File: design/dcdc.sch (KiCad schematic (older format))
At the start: 23 parts

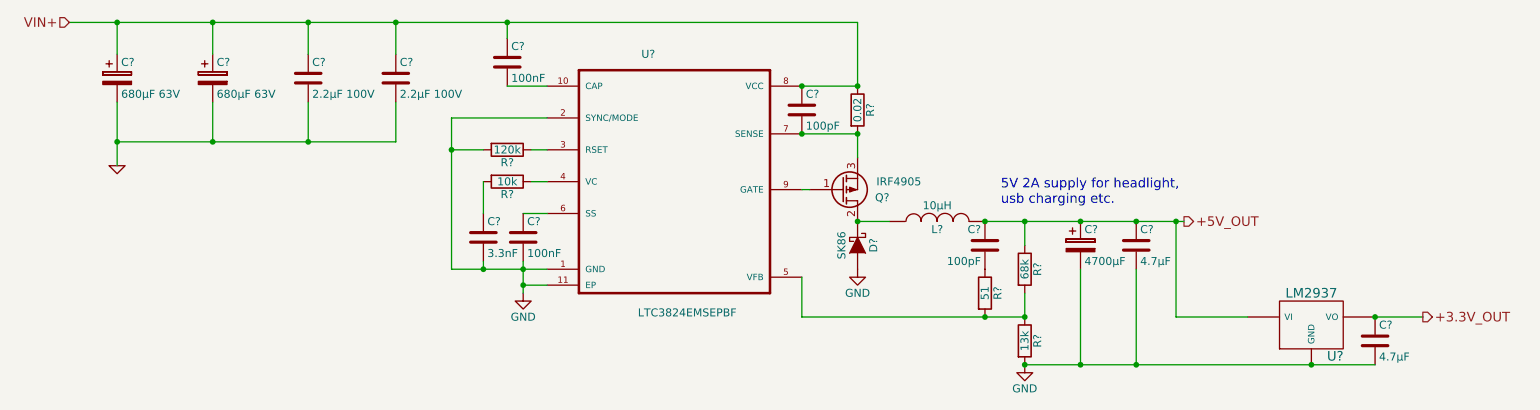
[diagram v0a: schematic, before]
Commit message: schema mods done
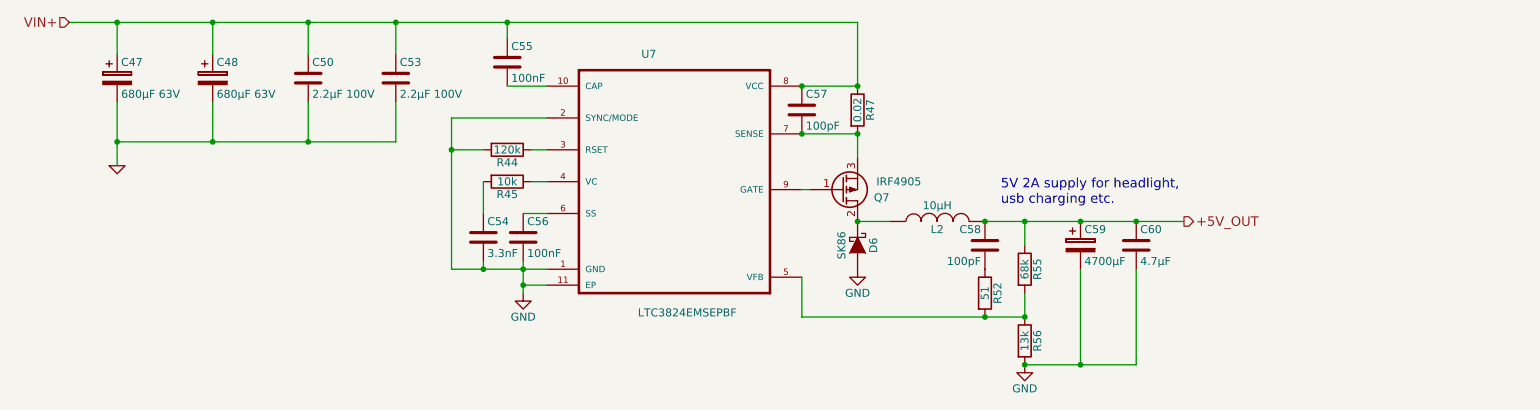
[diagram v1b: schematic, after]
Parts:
- removed C?: 4.7µF, Capacitors_SMD:C_1210, symbol C
- removed U?: LM2937, symbol LM2937
- gave numbers to parts that had none: 21
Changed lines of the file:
@@
 LIBS:LTC3824EMSEPBF
 LIBS:lm2937
+LIBS:bluetooth_spp-ca
+LIBS:microsd
+LIBS:lsm303d
+LIBS:lsm6ds3
 LIBS:BLDC_4-cache
 EELAYER 25 0
@@
 VIN+
 $Comp
-L CP C?
+L CP C47
 U 1 1 562DF65C
 P 1650 2500
-F 0 "C?" H 1675 2600 50  0000 L CNN
+F 0 "C47" H 1675 2600 50  0000 L CNN
 F 1 "680µF 63V" H 1675 2400 50  0000 L CNN
 F 2 "" H 1688 2350 30  0000 C CNN
@@
 $EndComp
 $Comp
-L CP C?
+L CP C48
 U 1 1 562DF6B6
 P 2250 2500
-F 0 "C?" H 2275 2600 50  0000 L CNN
+F 0 "C48" H 2275 2600 50  0000 L CNN
 F 1 "680µF 63V" H 2275 2400 50  0000 L CNN
 F 2 "" H 2288 2350 30  0000 C CNN
@@
 Connection ~ 1650 2900
 $Comp
-L LTC3824EMSEPBF-RESCUE-dcdc U?
+L LTC3824EMSEPBF-RESCUE-dcdc U7
 U 1 1 562DF9A8
 P 5150 3050
-F 0 "U?" H 4942 3751 50  0000 L CNN
+F 0 "U7" H 4942 3751 50  0000 L CNN
 F 1 "LTC3824EMSEPBF" H 4920 2127 50  0000 L CNN
 F 2 "SOP50P490X110-11N" H 4900 2050 50  0001 L CNN
@@
 +5V_OUT
 $Comp
-L GND-RESCUE-BLDC_4 #PWR?
+L GND-RESCUE-BLDC_4 #PWR079
 U 1 1 562F6985
 P 1650 3050
-F 0 "#PWR?" H 1650 3050 30  0001 C CNN
+F 0 "#PWR079" H 1650 3050 30  0001 C CNN
 F 1 "GND-RESCUE-BLDC_4" H 1650 2980 30  0001 C CNN
 F 2 "" H 1650 3050 60  0000 C CNN
@@
 	1650 2900 3400 2900
 $Comp
-L C C?
+L C C55
 U 1 1 562F82C1
 P 4100 2400
-F 0 "C?" H 4125 2500 50  0000 L CNN
+F 0 "C55" H 4125 2500 50  0000 L CNN
 F 1 "100nF" H 4125 2300 50  0000 L CNN
 F 2 "" H 4138 2250 30  0000 C CNN
@@
 Connection ~ 4100 2150
 $Comp
-L C C?
+L C C57
 U 1 1 562F83DF
 P 5950 2700
-F 0 "C?" H 5975 2800 50  0000 L CNN
+F 0 "C57" H 5975 2800 50  0000 L CNN
 F 1 "100pF" H 5975 2600 50  0000 L CNN
 F 2 "" H 5988 2550 30  0000 C CNN
@@
 Connection ~ 5950 2550
 $Comp
-L R R?
+L R R47
 U 1 1 562F843B
 P 6300 2700
-F 0 "R?" V 6380 2700 50  0000 C CNN
+F 0 "R47" V 6380 2700 50  0000 C CNN
 F 1 "0.02" V 6300 2700 50  0000 C CNN
 F 2 "" V 6230 2700 30  0000 C CNN
@@
 Connection ~ 5950 2850
 $Comp
-L Q_PMOS_GDS Q?
+L Q_PMOS_GDS Q7
 U 1 1 562F8883
 P 6200 3200
-F 0 "Q?" H 6500 3250 50  0000 R CNN
+F 0 "Q7" H 6500 3250 50  0000 R CNN
 F 1 "IRF4905" H 6700 3150 50  0000 R CNN
 F 2 "TO_SOT_Packages_SMD:TO-252-2Lead" H 6400 3300 29  0001 C CNN
@@
 $EndComp
 $Comp
-L D_Schottky D?
+L D_Schottky D6
 U 1 1 562F8884
 P 6300 3550
-F 0 "D?" H 6300 3650 50  0000 C CNN
+F 0 "D6" H 6300 3650 50  0000 C CNN
 F 1 "SK86" H 6300 3450 50  0000 C CNN
 F 2 "Diodes_SMD:SMC_Standard" H 6300 3550 60  0001 C CNN
@@
 $EndComp
 $Comp
-L GND #PWR?
+L GND #PWR080
 U 1 1 562F8885
 P 6300 3700
-F 0 "#PWR?" H 6300 3450 50  0001 C CNN
+F 0 "#PWR080" H 6300 3450 50  0001 C CNN
 F 1 "GND" H 6300 3550 50  0000 C CNN
 F 2 "" H 6300 3700 60  0000 C CNN
@@
 $EndComp
 $Comp
-L INDUCTOR L?
+L INDUCTOR L2
 U 1 1 562F8886
 P 6800 3400
-F 0 "L?" V 6750 3400 50  0000 C CNN
+F 0 "L2" V 6750 3400 50  0000 C CNN
 F 1 "10µH" V 6900 3400 50  0000 C CNN
 F 2 "DL50-10:DL50-10" H 6800 3400 60  0001 C CNN
@@
 $EndComp
 $Comp
-L C C?
+L C C58
 U 1 1 562F8887
 P 7100 3550
-F 0 "C?" H 7125 3650 50  0000 L CNN
+F 0 "C58" H 7125 3650 50  0000 L CNN
 F 1 "100pF" H 7125 3450 50  0000 L CNN
 F 2 "Capacitors_SMD:C_0402" H 7138 3400 30  0001 C CNN
@@
 $EndComp
 $Comp
-L R R?
+L R R52
 U 1 1 562F8888
 P 7100 3850
-F 0 "R?" V 7180 3850 50  0000 C CNN
+F 0 "R52" V 7180 3850 50  0000 C CNN
 F 1 "51" V 7100 3850 50  0000 C CNN
 F 2 "Resistors_SMD:R_0402" V 7030 3850 30  0001 C CNN
@@
 $EndComp
 $Comp
-L R R?
+L R R55
 U 1 1 562F8889
 P 7350 3700
-F 0 "R?" V 7430 3700 50  0000 C CNN
+F 0 "R55" V 7430 3700 50  0000 C CNN
 F 1 "68k" V 7350 3700 50  0000 C CNN
 F 2 "Resistors_SMD:R_0402" V 7280 3700 30  0001 C CNN
@@
 $EndComp
 $Comp
-L R R?
+L R R56
 U 1 1 562F888A
 P 7350 4150
-F 0 "R?" V 7430 4150 50  0000 C CNN
+F 0 "R56" V 7430 4150 50  0000 C CNN
 F 1 "13k" V 7350 4150 50  0000 C CNN
 F 2 "Resistors_SMD:R_0402" V 7280 4150 30  0001 C CNN
@@
 $EndComp
 $Comp
-L GND #PWR?
+L GND #PWR081
 U 1 1 562F888B
 P 7350 4300
-F 0 "#PWR?" H 7350 4050 50  0001 C CNN
+F 0 "#PWR081" H 7350 4050 50  0001 C CNN
 F 1 "GND" H 7350 4150 50  0000 C CNN
 F 2 "" H 7350 4300 60  0000 C CNN
@@
 $EndComp
 $Comp
-L CP C?
+L CP C59
 U 1 1 562F888C
 P 7700 3550
-F 0 "C?" H 7725 3650 50  0000 L CNN
+F 0 "C59" H 7725 3650 50  0000 L CNN
 F 1 "4700µF" H 7725 3450 50  0000 L CNN
 F 2 "Capacitors_Elko_ThroughHole:Elko_vert_31.5x16mm_RM7.5" H 7738 3400 30  0001 C CNN
@@
 $EndComp
 $Comp
-L C C?
+L C C56
 U 1 1 562F8890
 P 4200 3500
-F 0 "C?" H 4225 3600 50  0000 L CNN
+F 0 "C56" H 4225 3600 50  0000 L CNN
 F 1 "100nF" H 4225 3400 50  0000 L CNN
 F 2 "Capacitors_SMD:C_0402" H 4238 3350 30  0001 C CNN
@@
 $EndComp
 $Comp
-L C C?
+L C C54
 U 1 1 562F8891
 P 3950 3500
-F 0 "C?" H 3975 3600 50  0000 L CNN
+F 0 "C54" H 3975 3600 50  0000 L CNN
 F 1 "3.3nF" H 3975 3400 50  0000 L CNN
 F 2 "Capacitors_SMD:C_0402" H 3988 3350 30  0001 C CNN
@@
 $EndComp
 $Comp
-L R R?
+L R R45
 U 1 1 562F8892
 P 4100 3150
-F 0 "R?" V 4180 3150 50  0000 C CNN
+F 0 "R45" V 4180 3150 50  0000 C CNN
 F 1 "10k" V 4100 3150 50  0000 C CNN
 F 2 "Resistors_SMD:R_0402" V 4030 3150 30  0001 C CNN
@@
 	3950 3700 3950 3650
 $Comp
-L R R?
+L R R44
 U 1 1 562F8893
 P 4100 2950
-F 0 "R?" V 4180 2950 50  0000 C CNN
+F 0 "R44" V 4180 2950 50  0000 C CNN
 F 1 "120k" V 4100 2950 50  0000 C CNN
 F 2 "Resistors_SMD:R_0402" V 4030 2950 30  0001 C CNN
@@
 Connection ~ 3750 2950
 $Comp
-L GND #PWR?
+L GND #PWR082
 U 1 1 562F8896
 P 4200 3850
-F 0 "#PWR?" H 4200 3600 50  0001 C CNN
+F 0 "#PWR082" H 4200 3600 50  0001 C CNN
 F 1 "GND" H 4200 3700 50  0000 C CNN
 F 2 "" H 4200 3850 60  0000 C CNN
@@
 Connection ~ 4200 3800
 $Comp
-L C C?
+L C C50
 U 1 1 562F889B
 P 2850 2500
-F 0 "C?" H 2875 2600 50  0000 L CNN
+F 0 "C50" H 2875 2600 50  0000 L CNN
 F 1 "2.2µF 100V" H 2875 2400 50  0000 L CNN
 F 2 "Capacitors_SMD:C_1210" H 2888 2350 30  0001 C CNN
@@
 $EndComp
 $Comp
-L C C?
+L C C60
 U 1 1 562F889C
 P 8050 3550
-F 0 "C?" H 8075 3650 50  0000 L CNN
+F 0 "C60" H 8075 3650 50  0000 L CNN
 F 1 "4.7µF" H 8075 3450 50  0000 L CNN
 F 2 "Capacitors_SMD:C_1210" H 8088 3400 30  0001 C CNN
@@
 Connection ~ 8050 3400
 $Comp
-L C C?
+L C C53
 U 1 1 562F8C6C
 P 3400 2500
-F 0 "C?" H 3425 2600 50  0000 L CNN
+F 0 "C53" H 3425 2600 50  0000 L CNN
 F 1 "2.2µF 100V" H 3425 2400 50  0000 L CNN
 F 2 "Capacitors_SMD:C_1210" H 3438 2350 30  0001 C CNN
@@
 Wire Wire Line
 	7700 3700 7700 4300
-Wire Wire Line
-	7350 4300 9550 4300
 Connection ~ 7350 4300
 Wire Wire Line
@@
 Text Notes 7200 3300 0    60   ~ 0
 5V 2A supply for headlight,\nusb charging etc.
-$Comp
-L LM2937 U?
-U 1 1 562FC7C9
-P 9150 4050
-F 0 "U?" H 9300 3854 60  0000 C CNN
-F 1 "LM2937" H 9150 4250 60  0000 C CNN
-F 2 "" H 9150 4050 60  0000 C CNN
-F 3 "" H 9150 4050 60  0000 C CNN
-	1    9150 4050
-	1    0    0    -1
-$EndComp
-$Comp
-L C C?
-U 1 1 562FC8CC
-P 9550 4150
-F 0 "C?" H 9575 4250 50  0000 L CNN
-F 1 "4.7µF" H 9575 4050 50  0000 L CNN
-F 2 "Capacitors_SMD:C_1210" H 9588 4000 30  0001 C CNN
-F 3 "" H 9550 4150 60  0000 C CNN
-	1    9550 4150
-	1    0    0    -1
-$EndComp
-Connection ~ 8050 4300
-Connection ~ 9150 4300
-Wire Wire Line
-	8750 4000 8300 4000
-Wire Wire Line
-	8300 4000 8300 3400
-Connection ~ 8300 3400
-Text HLabel 9850 4000 2    60   Output ~ 0
-+3.3V_OUT
-Wire Wire Line
-	9850 4000 9550 4000
-Connection ~ 9550 4000
+Wire Wire Line
+	7350 4300 8050 4300
 $EndSCHEMATC
